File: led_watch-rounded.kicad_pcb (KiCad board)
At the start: 4 copper layers, 29 x 29 mm, 95 parts, among them U3 M0G3507QDGS32RQ1, Y2 TXC-7C

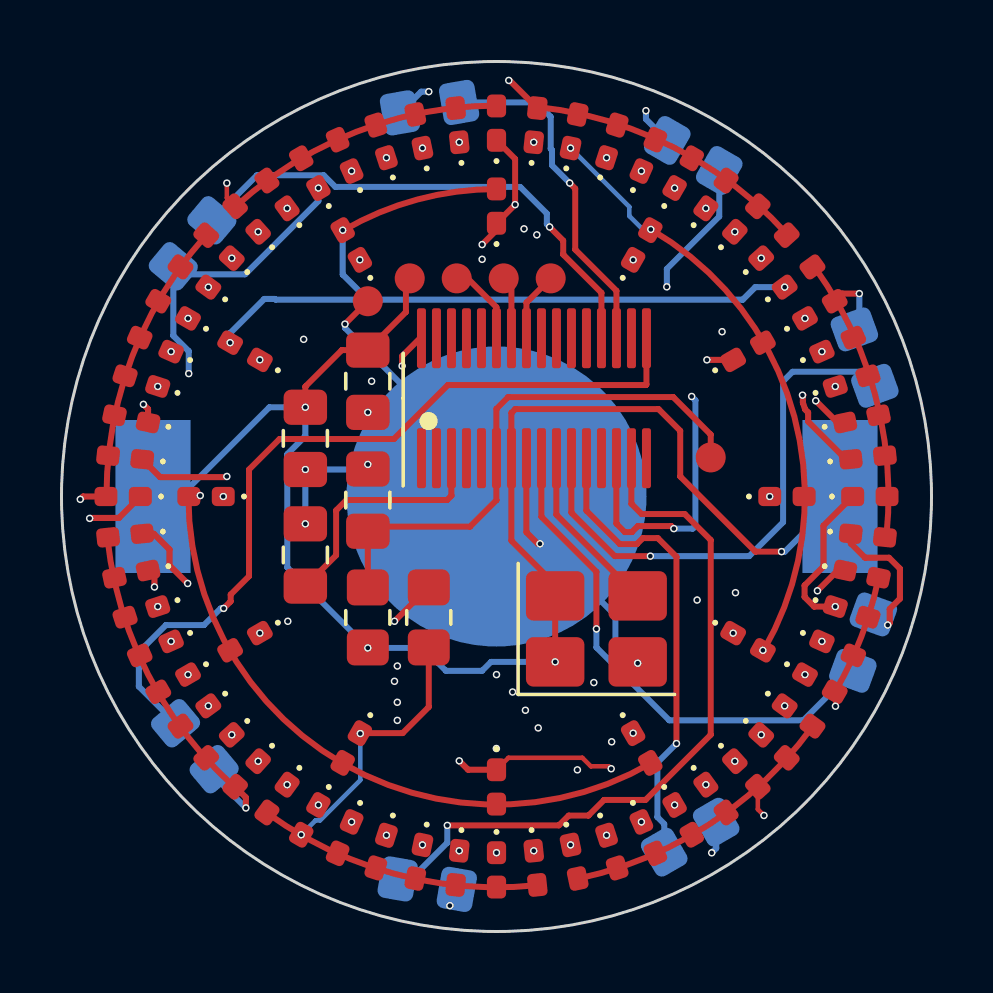
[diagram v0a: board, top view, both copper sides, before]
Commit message: rounded tracks
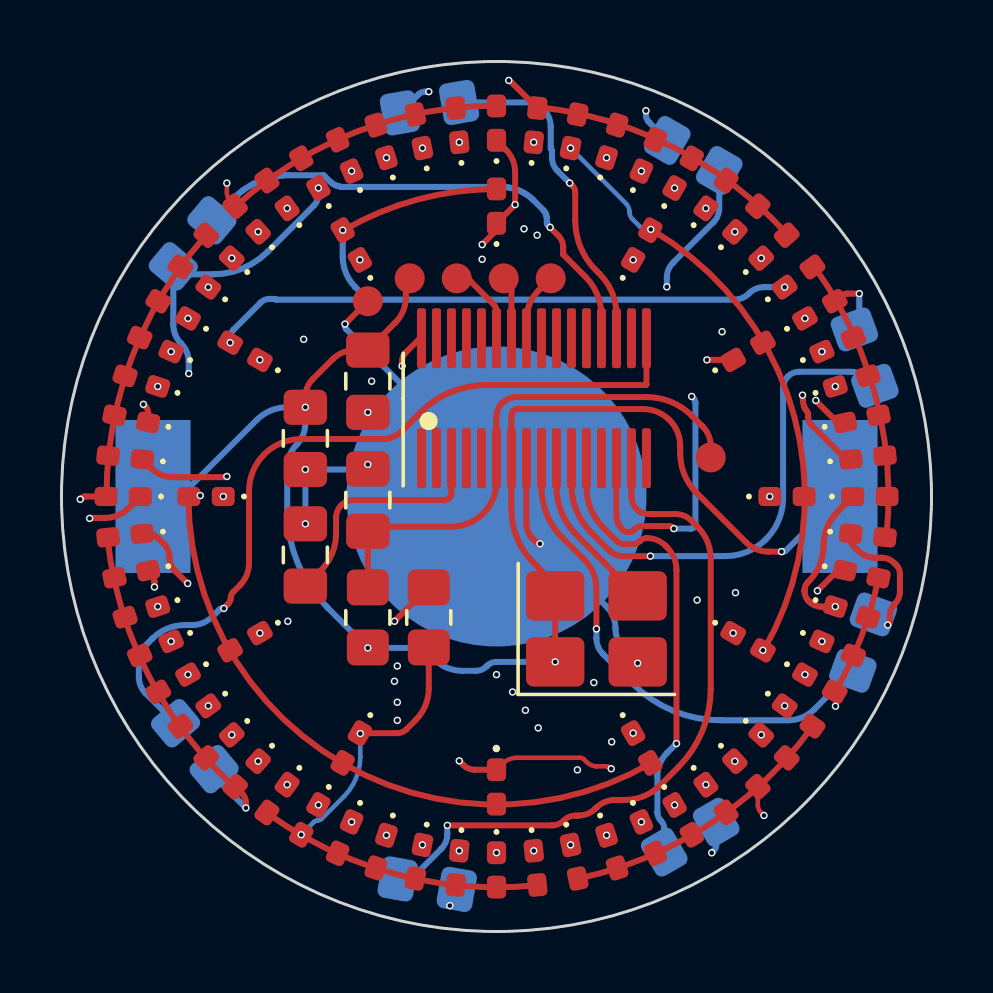
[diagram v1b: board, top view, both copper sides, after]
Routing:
- net +VBATT: track 52.2 -> 48.9 mm
- net PA5/HFXIN: track 104.6 -> 102.0 mm
- net PA13/TFT_D/C: track 75.4 -> 73.2 mm
- net NRST: track 18.0 -> 15.8 mm
- net GND: track 28.1 -> 25.9 mm
- net PA4: track 82.0 -> 79.9 mm
- net PA10: track 82.2 -> 80.2 mm
- net PA2: track 83.3 -> 81.6 mm
- net PA7: track 112.7 -> 111.1 mm
- net Net-(U3-PA13): track 17.2 -> 16.1 mm
- net Net-(U3-PA12/FCC_IN): track 11.5 -> 10.5 mm
- net Net-(U3-PA8): track 23.9 -> 23.1 mm
- net Net-(U3-PA4/LFCLK_IN/LFXOUT): track 18.0 -> 17.3 mm
- net SWCLK: track 2.67 -> 1.98 mm
- net PA18/SPI1_PICO/BSL_Invoke: track 2.33 -> 1.65 mm
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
